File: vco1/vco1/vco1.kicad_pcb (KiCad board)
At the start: 4 copper layers, 30 x 128.5 mm, 83 parts, among them J1 Conn_02x08_Odd_Even, Q1 DNP, SW1 SW_SPDT, U1 SSI2131, U2 TL431BCDBZR, U4 TL072HxD, U5 TL072HxD

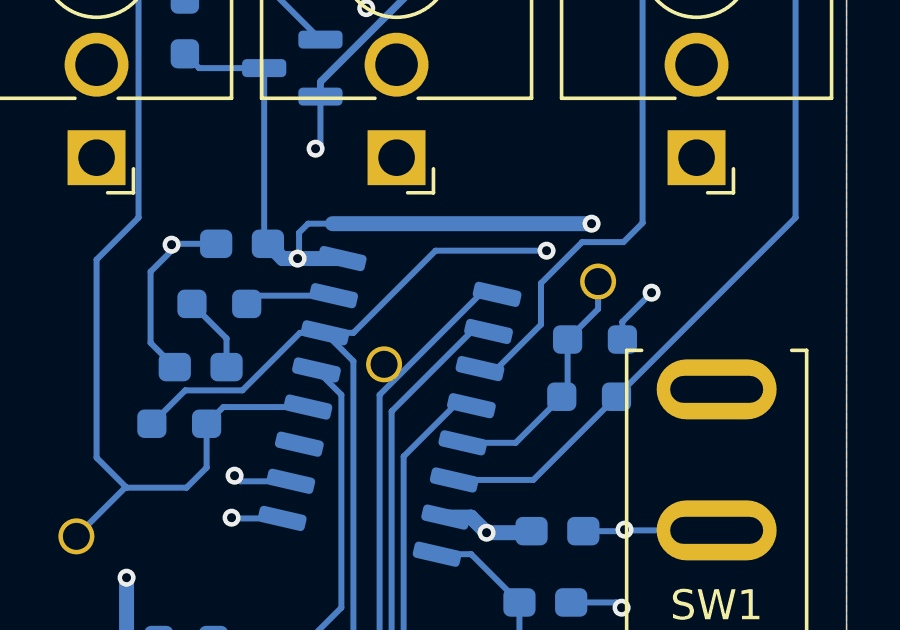
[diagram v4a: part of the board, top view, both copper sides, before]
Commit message: VCO prototype 1 to Aisler
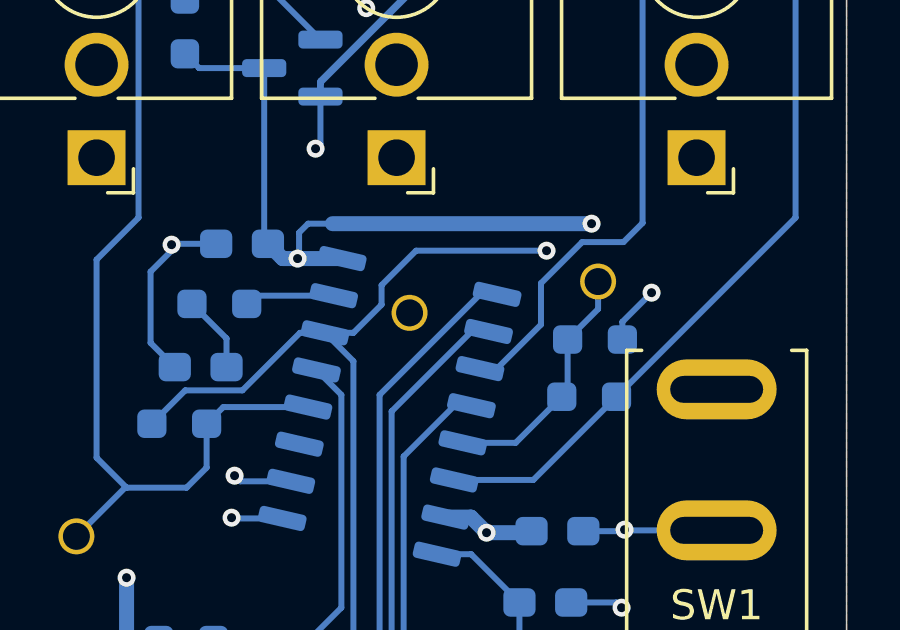
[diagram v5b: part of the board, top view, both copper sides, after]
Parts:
- moved TP7 1.91 mm to (90.4, 100.2)
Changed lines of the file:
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@@
 	(footprint "Holes:TP_0.9mm"
 		(layer "F.Cu")
-		(at 89.583404 101.887701)
+		(at 90.433182 100.171975)
 		(descr "THT pad as test Point, diameter 1.5mm, hole diameter 0.7mm")
 		(tags "test point THT pad")
@@
 	)
 	(segment
+		(start 89.5 99.25)
+		(end 90.65 98.1)
+		(width 0.2)
+		(layer "B.Cu")
+		(net 12)
+	)
+	(segment
 		(start 88.561217 113.438783)
 		(end 86.519 115.481)
@@
 	)
 	(segment
-		(start 83.897715 114.711628)
-		(end 84.667087 115.481)
+		(start 87.615871 100.837974)
+		(end 88.562026 100.837974)
 		(width 0.2)
 		(layer "B.Cu")
@@
 	)
 	(segment
-		(start 95.232305 117.192453)
-		(end 93.376043 117.192453)
+		(start 83.897715 114.711628)
+		(end 84.667087 115.481)
 		(width 0.2)
 		(layer "B.Cu")
@@
 	)
 	(segment
-		(start 87.615871 100.837974)
-		(end 88.561217 101.78332)
+		(start 95.232305 117.192453)
+		(end 93.376043 117.192453)
 		(width 0.2)
 		(layer "B.Cu")
@@
 	(segment
 		(start 87.615871 100.837974)
-		(end 88.562026 100.837974)
+		(end 88.561217 101.78332)
 		(width 0.2)
 		(layer "B.Cu")
@@
 	)
 	(segment
-		(start 88.562026 100.837974)
-		(end 91.3 98.1)
-		(width 0.2)
-		(layer "B.Cu")
-		(net 12)
-	)
-	(segment
 		(start 95.721955 119.863592)
 		(end 97.336408 119.863592)
@@
 	)
 	(segment
+		(start 88.562026 100.837974)
+		(end 89.5 99.9)
+		(width 0.2)
+		(layer "B.Cu")
+		(net 12)
+	)
+	(segment
+		(start 90.65 98.1)
+		(end 95 98.1)
+		(width 0.2)
+		(layer "B.Cu")
+		(net 12)
+	)
+	(segment
 		(start 84.861503 102.756352)
 		(end 82.955537 102.756352)
@@
 	)
 	(segment
-		(start 91.3 98.1)
-		(end 95 98.1)
+		(start 89.5 99.9)
+		(end 89.5 99.25)
 		(width 0.2)
 		(layer "B.Cu")
